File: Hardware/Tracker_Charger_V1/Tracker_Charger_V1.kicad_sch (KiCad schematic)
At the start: 145 parts, among them J1 USB_C_USB20, J2 GSB3CN1130DSHR, J3 GSB3CN1130DSHR, J4 GSB3CN1130DSHR, J5 SSD1306_I2C_128x64, J6 GSB3CN1130DSHR, J7 GSB3CN1130DSHR, J8 ST-LINK, SW1 SW_Push, SW2 SW_Push, SW3 SW_Push, SW4 SW_Push, SW5 SW_Push, SW6 SW_Push, U1 FT234XD-T, U10 INA180A3, U11 INA180A3, U12 INA180A3, U13 INA180A3, U2 IN-PI15TAT5R5G5B, U3 RT8010, U4 STM32G070CBTx, U5 INA180A3, U6 IN-PI15TAT5R5G5B, U7 IN-PI15TAT5R5G5B, U8 IN-PI15TAT5R5G5B, U9 IN-PI15TAT5R5G5B, Y1 8MHz

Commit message: Finalized PCBs & Generated Gerbers
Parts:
- added LG4: ~, 00_tracker_fp:mountains1, symbol 00_tracker_sym:LOGO_MISC
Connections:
- no-connect marks 72 -> 81
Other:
- note added: "Buck = ((3.3V*200mA)/95%)/4.8V = 145mA Charger Ports = 400mA each Expected Total = 145mA+400mA*5 = 2145mA (Within rating of regular 2.4A USB supply)"
- note added: "Fixed 3.3V buck, 1A Iout, 100% bypass mode Vin<Vout Max draw: 75mA + 40mA + 10mA = 125mA Eff@ 200mA = 96%, Pd = 28mW Bypass resistance: RdsOn = 0R3, RL = 0R144 Min 3Vout@200mA, 3V + 200mA * 0R588 = 3.12V min Vin"
- note added: "Max draw = 10mA"
- note added: "Max draw = 40mA"
- note removed: "Fixed 3.3V buck, 1A Iout, 100% bypass mode Vin<Vout Expected draw: 120mA + 10mA + 30mA = 160mA Peak draw: 500mA + 15mA + 60mA = 575mA Eff@ 200mA = 96%, Pd = 28mW Eff@ 600mA = 93%, Pd = 150mW Bypass resistance: RdsOn = 0R3, RL = 0R144 Min 3Vout@575mA, 3V + 0.575A * 0R444 = 3.26V min Vin"
- moved on the sheet: LG5, LG6
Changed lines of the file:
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@@
   (no_connect (at 78.74 339.09))
   (no_connect (at 269.24 323.85))
+  (no_connect (at 466.09 140.97))
   (no_connect (at 43.18 321.31))
   (no_connect (at 269.24 339.09))
@@
   (no_connect (at 191.77 334.01))
   (no_connect (at 325.12 121.92))
+  (no_connect (at 496.57 133.35))
   (no_connect (at 156.21 336.55))
   (no_connect (at 417.83 336.55))
@@
   (no_connect (at 43.18 323.85))
   (no_connect (at 269.24 336.55))
+  (no_connect (at 466.09 148.59))
   (no_connect (at 304.8 339.09))
   (no_connect (at 43.18 336.55))
+  (no_connect (at 496.57 135.89))
   (no_connect (at 191.77 328.93))
   (no_connect (at 304.8 323.85))
@@
   (no_connect (at 382.27 323.85))
   (no_connect (at 269.24 321.31))
+  (no_connect (at 466.09 151.13))
   (no_connect (at 530.86 339.09))
   (no_connect (at 325.12 124.46))
@@
   (no_connect (at 382.27 339.09))
   (no_connect (at 530.86 321.31))
+  (no_connect (at 496.57 148.59))
   (no_connect (at 304.8 334.01))
   (no_connect (at 269.24 331.47))
@@
   (no_connect (at 382.27 321.31))
   (no_connect (at 417.83 321.31))
+  (no_connect (at 466.09 143.51))
   (no_connect (at 495.3 336.55))
   (no_connect (at 97.79 86.36))
   (no_connect (at 530.86 328.93))
   (no_connect (at 102.87 218.44))
+  (no_connect (at 496.57 156.21))
   (no_connect (at 156.21 331.47))
   (no_connect (at 97.79 83.82))
@@
   (no_connect (at 78.74 323.85))
   (no_connect (at 191.77 321.31))
+  (no_connect (at 466.09 146.05))
   (no_connect (at 198.12 171.45))
   (no_connect (at 78.74 321.31))
@@
     (effects (font (size 1.27 1.27)) (justify left bottom))
   )
-  (text "Fixed 3.3V buck, 1A Iout, 100% bypass mode Vin<Vout\n\nExpected draw: 120mA + 10mA + 30mA = 160mA\nPeak draw:     500mA + 15mA + 60mA = 575mA\n\nEff@ 200mA = 96%, Pd = 28mW\nEff@ 600mA = 93%, Pd = 150mW\n\nBypass resistance: RdsOn = 0R3, RL = 0R144\nMin 3Vout@575mA, 3V + 0.575A * 0R444 = 3.26V min Vin"
+  (text "Max draw = 40mA" (at 261.62 193.04 0)
+    (effects (font (size 1.27 1.27)) (justify left bottom))
+  )
+  (text "Fixed 3.3V buck, 1A Iout, 100% bypass mode Vin<Vout\n\nMax draw: 75mA + 40mA + 10mA = 125mA\n\nEff@ 200mA = 96%, Pd = 28mW\n\nBypass resistance: RdsOn = 0R3, RL = 0R144\nMin 3Vout@200mA, 3V + 200mA * 0R588 = 3.12V min Vin"
     (at 161.29 63.5 0)
     (effects (font (size 1.27 1.27)) (justify left bottom))
@@
     (effects (font (size 1.27 1.27)) (justify left bottom))
   )
+  (text "Buck = ((3.3V*200mA)/95%)/4.8V = 145mA\nCharger Ports = 400mA each\nExpected Total = 145mA+400mA*5 = 2145mA\n(Within rating of regular 2.4A USB supply)"
+    (at 80.01 49.53 0)
+    (effects (font (size 1.27 1.27)) (justify left bottom))
+  )
   (text "I2C1" (at 481.33 176.53 0)
     (effects (font (size 1.27 1.27)) (justify left bottom))
@@
     (effects (font (size 1.27 1.27)) (justify left bottom))
   )
+  (text "Max draw = 10mA" (at 466.09 77.47 0)
+    (effects (font (size 1.27 1.27)) (justify left bottom))
+  )
   (text "USART3" (at 481.33 181.61 0)
     (effects (font (size 1.27 1.27)) (justify left bottom))
@@
     )
   )
+  (symbol (lib_id "00_tracker_sym:LOGO_MISC") (at 128.27 217.17 0) (unit 1)
+    (in_bom yes) (on_board yes) (dnp no) (fields_autoplaced)
+    (property "Reference" "LG4" (at 134.62 219.71 0)
+      (effects (font (size 1.27 1.27)) (justify left))
+    )
+    (property "Value" "~" (at 128.27 215.9 0)
+      (effects (font (size 1.27 1.27)))
+    )
+    (property "Footprint" "00_tracker_fp:mountains1" (at 128.27 215.9 0)
+      (effects (font (size 1.27 1.27)) hide)
+    )
+    (property "Datasheet" "" (at 128.27 215.9 0)
+      (effects (font (size 1.27 1.27)) hide)
+    )
+    (instances
+      (project "Tracker_Charger_V1"
+        (path "/38c4babf-9cde-4e06-a603-1df616028c2e"
+          (reference "LG4") (unit 1)
+        )
+      )
+    )
+  )
   (symbol (lib_id "power:GND") (at 168.91 287.02 0) (mirror y) (unit 1)
     (in_bom yes) (on_board yes) (dnp no)
@@
     )
   )
-  (symbol (lib_id "00_tracker_sym:LOGO_MISC") (at 128.27 223.52 0) (unit 1)
+  (symbol (lib_id "00_tracker_sym:LOGO_MISC") (at 128.27 229.87 0) (unit 1)
     (in_bom yes) (on_board yes) (dnp no) (fields_autoplaced)
-    (property "Reference" "LG6" (at 134.62 226.06 0)
+    (property "Reference" "LG6" (at 134.62 232.41 0)
       (effects (font (size 1.27 1.27)) (justify left))
     )
-    (property "Value" "~" (at 128.27 222.25 0)
+    (property "Value" "~" (at 128.27 228.6 0)
       (effects (font (size 1.27 1.27)))
     )
-    (property "Footprint" "00_tracker_fp:squat_silk_14mm" (at 128.27 222.25 0)
+    (property "Footprint" "00_tracker_fp:squat_silk_14mm" (at 128.27 228.6 0)
       (effects (font (size 1.27 1.27)) hide)
     )
-    (property "Datasheet" "" (at 128.27 222.25 0)
+    (property "Datasheet" "" (at 128.27 228.6 0)
       (effects (font (size 1.27 1.27)) hide)
     )
@@
     )
   )
-  (symbol (lib_id "00_tracker_sym:LOGO_MISC") (at 128.27 217.17 0) (unit 1)
+  (symbol (lib_id "00_tracker_sym:LOGO_MISC") (at 128.27 223.52 0) (unit 1)
     (in_bom yes) (on_board yes) (dnp no) (fields_autoplaced)
-    (property "Reference" "LG5" (at 134.62 219.71 0)
+    (property "Reference" "LG5" (at 134.62 226.06 0)
       (effects (font (size 1.27 1.27)) (justify left))
     )
-    (property "Value" "~" (at 128.27 215.9 0)
+    (property "Value" "~" (at 128.27 222.25 0)
       (effects (font (size 1.27 1.27)))
     )
-    (property "Footprint" "00_tracker_fp:hike_silk_14mm" (at 128.27 215.9 0)
+    (property "Footprint" "00_tracker_fp:hike_silk_14mm" (at 128.27 222.25 0)
       (effects (font (size 1.27 1.27)) hide)
     )
-    (property "Datasheet" "" (at 128.27 215.9 0)
+    (property "Datasheet" "" (at 128.27 222.25 0)
       (effects (font (size 1.27 1.27)) hide)
     )

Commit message: Component ordering information finalized
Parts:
- H1, H2, H3, H4, H5, H6, JP1, JP2, JP3, JP4, JP5, JP6, LG1, LG2, LG3, LG4, LG5, LG6: now left out of the parts list
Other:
- note added: "Crystal load cap = 18p 27^2/2(27)+5 = 18.5p"
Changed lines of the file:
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@@
     (effects (font (size 1.27 1.27)) (justify left bottom))
   )
+  (text "Crystal load cap = 18p\n27^2/2(27)+5 = 18.5p" (at 417.83 172.72 0)
+    (effects (font (size 1.27 1.27)) (justify left bottom))
+  )
   (text "USART2" (at 481.33 118.11 0)
     (effects (font (size 1.27 1.27)) (justify left bottom))
@@
   )
   (symbol (lib_id "Jumper:SolderJumper_3_Open") (at 209.55 332.74 90) (unit 1)
-    (in_bom yes) (on_board yes) (dnp no)
+    (in_bom no) (on_board yes) (dnp no)
     (property "Reference" "JP3" (at 214.63 330.2 90)
       (effects (font (size 1.27 1.27)) (justify left))
@@
   )
   (symbol (lib_id "00_tracker_sym:LOGO_MISC") (at 128.27 217.17 0) (unit 1)
-    (in_bom yes) (on_board yes) (dnp no) (fields_autoplaced)
+    (in_bom no) (on_board yes) (dnp no) (fields_autoplaced)
     (property "Reference" "LG4" (at 134.62 219.71 0)
       (effects (font (size 1.27 1.27)) (justify left))
@@
   )
   (symbol (lib_id "Mechanical:MountingHole_Pad") (at 102.87 208.28 0) (unit 1)
-    (in_bom yes) (on_board yes) (dnp no) (fields_autoplaced)
+    (in_bom no) (on_board yes) (dnp no) (fields_autoplaced)
     (property "Reference" "H1" (at 105.41 205.74 0)
       (effects (font (size 1.27 1.27)) (justify left))
@@
   )
   (symbol (lib_id "Mechanical:MountingHole_Pad") (at 102.87 215.9 0) (unit 1)
-    (in_bom yes) (on_board yes) (dnp no) (fields_autoplaced)
+    (in_bom no) (on_board yes) (dnp no) (fields_autoplaced)
     (property "Reference" "H2" (at 105.41 213.36 0)
       (effects (font (size 1.27 1.27)) (justify left))
@@
   )
   (symbol (lib_id "Mechanical:MountingHole_Pad") (at 113.03 208.28 0) (unit 1)
-    (in_bom yes) (on_board yes) (dnp no) (fields_autoplaced)
+    (in_bom no) (on_board yes) (dnp no) (fields_autoplaced)
     (property "Reference" "H4" (at 115.57 205.74 0)
       (effects (font (size 1.27 1.27)) (justify left))
@@
   )
   (symbol (lib_id "Jumper:SolderJumper_3_Open") (at 322.58 332.74 90) (unit 1)
-    (in_bom yes) (on_board yes) (dnp no)
+    (in_bom no) (on_board yes) (dnp no)
     (property "Reference" "JP4" (at 327.66 330.2 90)
       (effects (font (size 1.27 1.27)) (justify left))
@@
   )
   (symbol (lib_id "Mechanical:MountingHole_Pad") (at 113.03 223.52 0) (unit 1)
-    (in_bom yes) (on_board yes) (dnp no) (fields_autoplaced)
+    (in_bom no) (on_board yes) (dnp no) (fields_autoplaced)
     (property "Reference" "H6" (at 115.57 220.98 0)
       (effects (font (size 1.27 1.27)) (justify left))
@@
   )
   (symbol (lib_id "00_tracker_sym:LOGO_MISC") (at 128.27 204.47 0) (unit 1)
-    (in_bom yes) (on_board yes) (dnp no) (fields_autoplaced)
+    (in_bom no) (on_board yes) (dnp no) (fields_autoplaced)
     (property "Reference" "LG2" (at 134.62 207.01 0)
       (effects (font (size 1.27 1.27)) (justify left))
@@
   )
   (symbol (lib_id "Mechanical:MountingHole_Pad") (at 102.87 223.52 0) (unit 1)
-    (in_bom yes) (on_board yes) (dnp no) (fields_autoplaced)
+    (in_bom no) (on_board yes) (dnp no) (fields_autoplaced)
     (property "Reference" "H3" (at 105.41 220.98 0)
       (effects (font (size 1.27 1.27)) (justify left))
@@
   )
   (symbol (lib_id "Jumper:SolderJumper_3_Open") (at 96.52 332.74 90) (unit 1)
-    (in_bom yes) (on_board yes) (dnp no)
+    (in_bom no) (on_board yes) (dnp no)
     (property "Reference" "JP2" (at 101.6 330.2 90)
       (effects (font (size 1.27 1.27)) (justify left))
@@
   )
   (symbol (lib_id "Mechanical:MountingHole_Pad") (at 113.03 215.9 0) (unit 1)
-    (in_bom yes) (on_board yes) (dnp no) (fields_autoplaced)
+    (in_bom no) (on_board yes) (dnp no) (fields_autoplaced)
     (property "Reference" "H5" (at 115.57 213.36 0)
       (effects (font (size 1.27 1.27)) (justify left))
@@
   )
   (symbol (lib_id "00_tracker_sym:LOGO_MISC") (at 128.27 229.87 0) (unit 1)
-    (in_bom yes) (on_board yes) (dnp no) (fields_autoplaced)
+    (in_bom no) (on_board yes) (dnp no) (fields_autoplaced)
     (property "Reference" "LG6" (at 134.62 232.41 0)
       (effects (font (size 1.27 1.27)) (justify left))
@@
   )
   (symbol (lib_id "Jumper:SolderJumper_3_Open") (at 435.61 332.74 90) (unit 1)
-    (in_bom yes) (on_board yes) (dnp no)
+    (in_bom no) (on_board yes) (dnp no)
     (property "Reference" "JP5" (at 440.69 330.2 90)
       (effects (font (size 1.27 1.27)) (justify left))
@@
   )
   (symbol (lib_id "00_tracker_sym:LOGO_MISC") (at 128.27 223.52 0) (unit 1)
-    (in_bom yes) (on_board yes) (dnp no) (fields_autoplaced)
+    (in_bom no) (on_board yes) (dnp no) (fields_autoplaced)
     (property "Reference" "LG5" (at 134.62 226.06 0)
       (effects (font (size 1.27 1.27)) (justify left))
@@
   )
   (symbol (lib_id "00_tracker_sym:LOGO_MISC") (at 128.27 210.82 0) (unit 1)
-    (in_bom yes) (on_board yes) (dnp no) (fields_autoplaced)
+    (in_bom no) (on_board yes) (dnp no) (fields_autoplaced)
     (property "Reference" "LG3" (at 134.62 213.36 0)
       (effects (font (size 1.27 1.27)) (justify left))
@@
   )
   (symbol (lib_id "Jumper:SolderJumper_3_Open") (at 250.19 196.85 90) (mirror x) (unit 1)
-    (in_bom yes) (on_board yes) (dnp no)
+    (in_bom no) (on_board yes) (dnp no)
     (property "Reference" "JP1" (at 256.54 194.31 90)
       (effects (font (size 1.27 1.27)) (justify left))
@@
   )
   (symbol (lib_id "00_tracker_sym:AB_LOGO") (at 571.5 379.73 0) (unit 1)
-    (in_bom yes) (on_board yes) (dnp no)
+    (in_bom no) (on_board yes) (dnp no)
     (property "Reference" "LG1" (at 568.96 379.73 0)
       (effects (font (size 1.27 1.27)) (justify left))
@@
   )
   (symbol (lib_id "Jumper:SolderJumper_3_Open") (at 548.64 332.74 90) (unit 1)
-    (in_bom yes) (on_board yes) (dnp no)
+    (in_bom no) (on_board yes) (dnp no)
     (property "Reference" "JP6" (at 553.72 330.2 90)
       (effects (font (size 1.27 1.27)) (justify left))

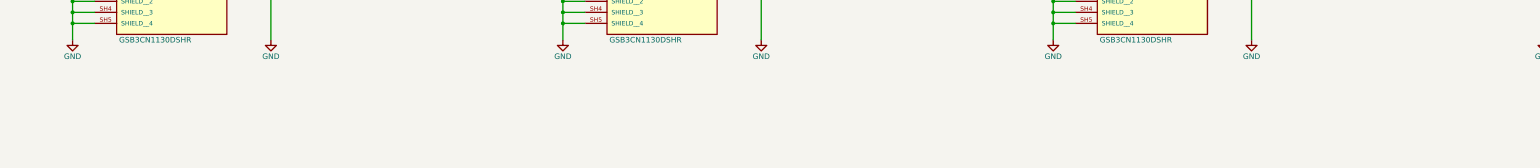
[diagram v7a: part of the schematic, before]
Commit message: Added incorrect FP warning
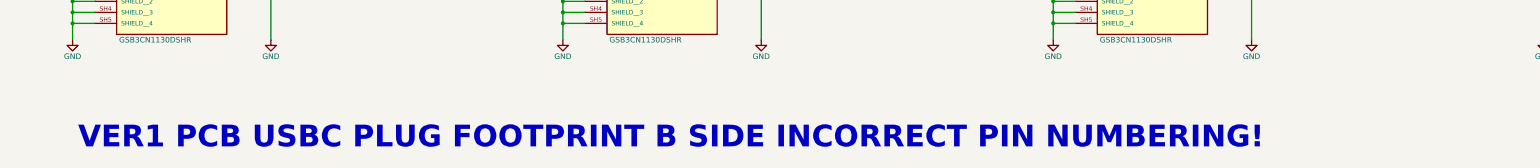
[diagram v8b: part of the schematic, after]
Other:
- note added: "VER1 PCB USBC PLUG FOOTPRINT B SIDE INCORRECT PIN NUMBERING!"
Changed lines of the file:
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@@
     (fill (type none))
+  )
+  (text "VER1 PCB USBC PLUG FOOTPRINT B SIDE INCORRECT PIN NUMBERING!"
+    (at 152.4 388.62 0)
+    (effects (font (size 5 5) (thickness 0.6) bold (color 198 23 0 1)) (justify left bottom))
   )
   (text "USART1" (at 481.33 171.45 0)
